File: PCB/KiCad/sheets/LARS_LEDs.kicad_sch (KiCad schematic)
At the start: 26 parts, among them J30 LED1, J31 LED2, SW2 User Button

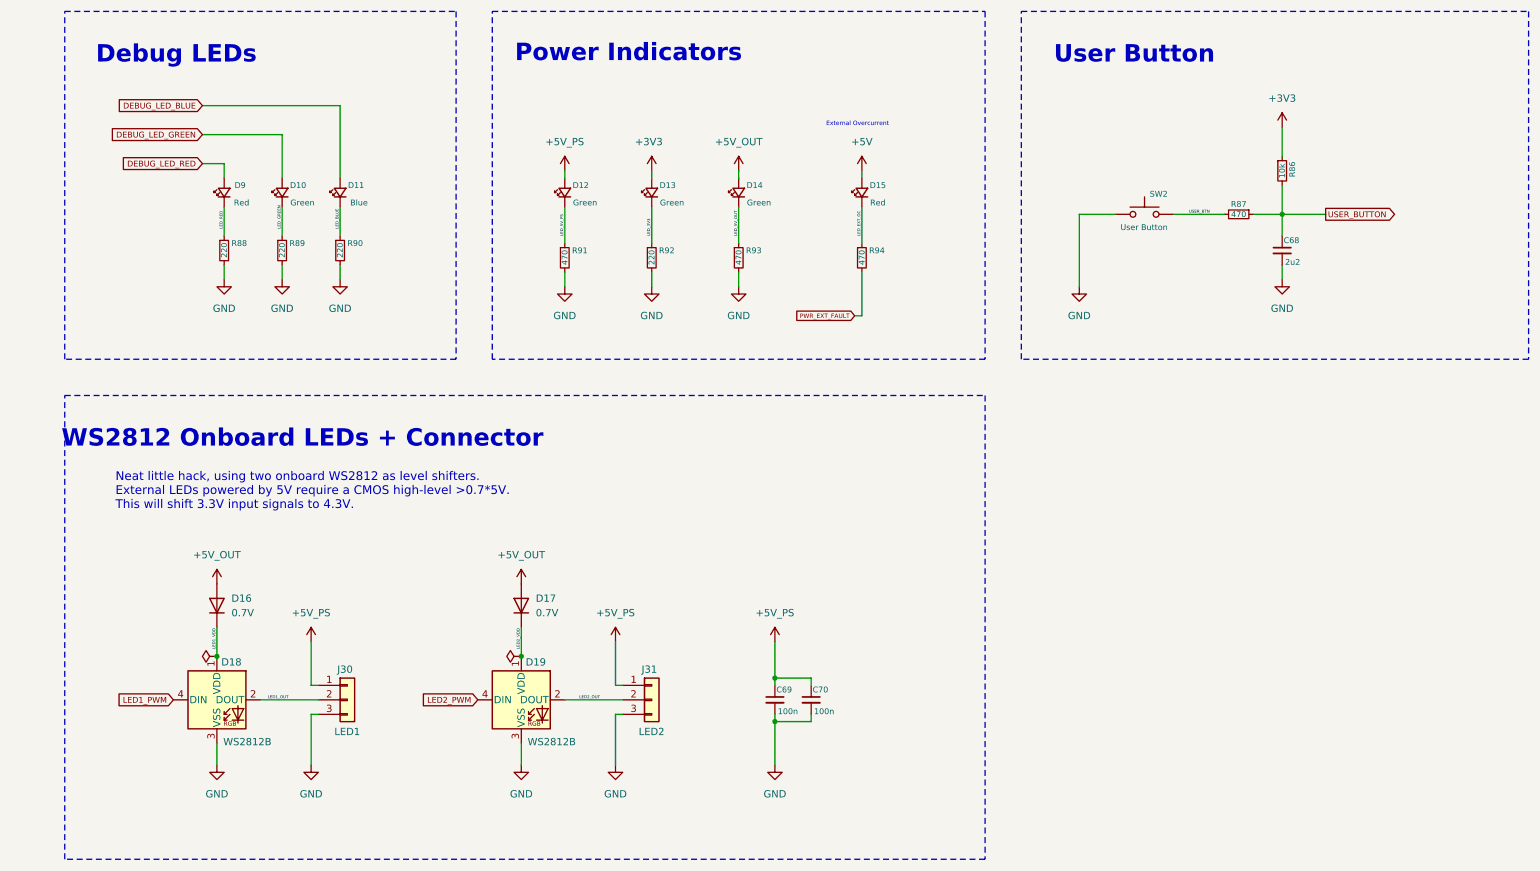
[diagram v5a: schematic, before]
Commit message: add ESD protection and update footprints
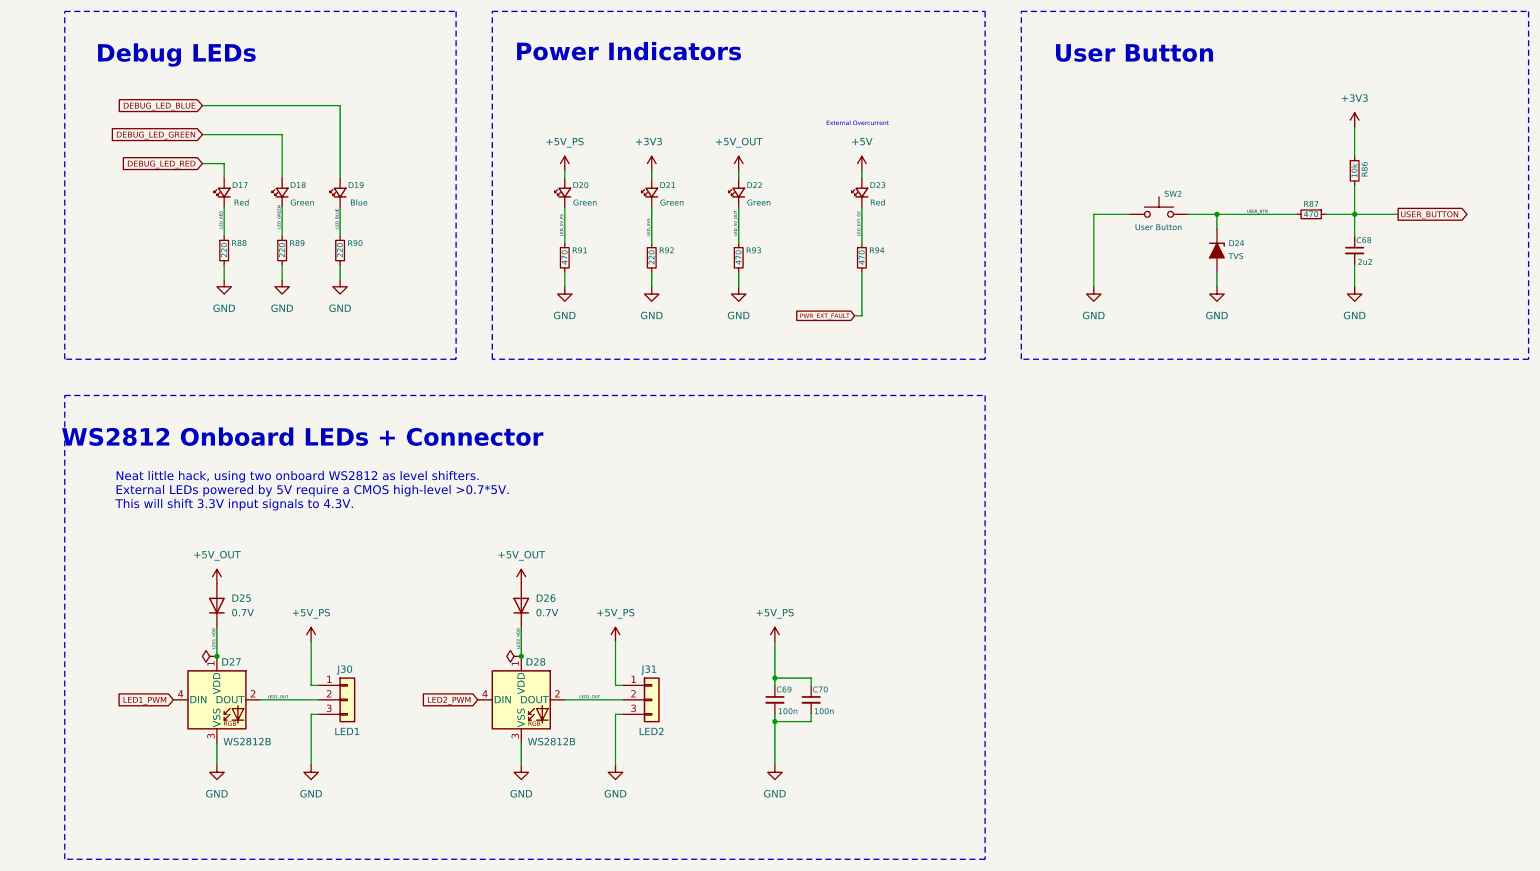
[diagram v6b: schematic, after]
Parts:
- added D24: TVS, LARS_Hardware_Interface:STS321050U182, symbol LARS_Hardware_Interface:D_TVS
- renumbered D9 to D17, D10 to D18, D11 to D19, D12 to D20, D13 to D21, D14 to D22, D15 to D23, D16 to D25, D17 to D26, D18 to D27, D19 to D28
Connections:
- net GND: now also D24.2 (A)
- net USER_BTN: now also D24.1 (K)
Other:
- moved on the sheet: C68, R86, R87, SW2

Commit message: PCB: update resistor values and embed font
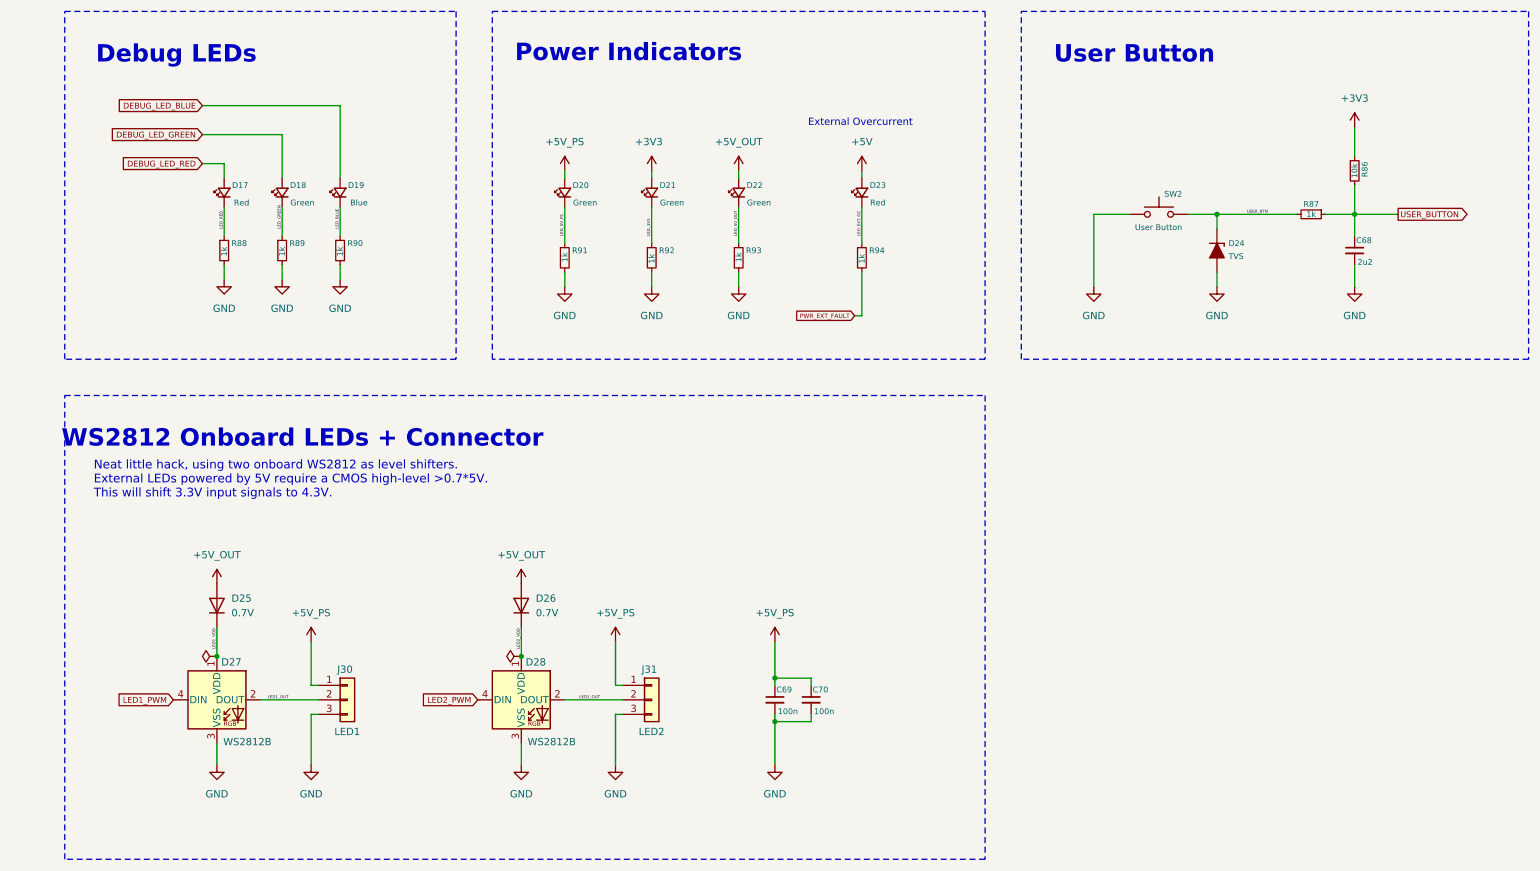
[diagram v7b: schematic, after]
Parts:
- R87, R91, R93, R94: value 470 -> 1k
- R88, R89, R90, R92: value 220 -> 1k
